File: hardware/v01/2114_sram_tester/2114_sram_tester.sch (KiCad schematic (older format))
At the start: 4 parts

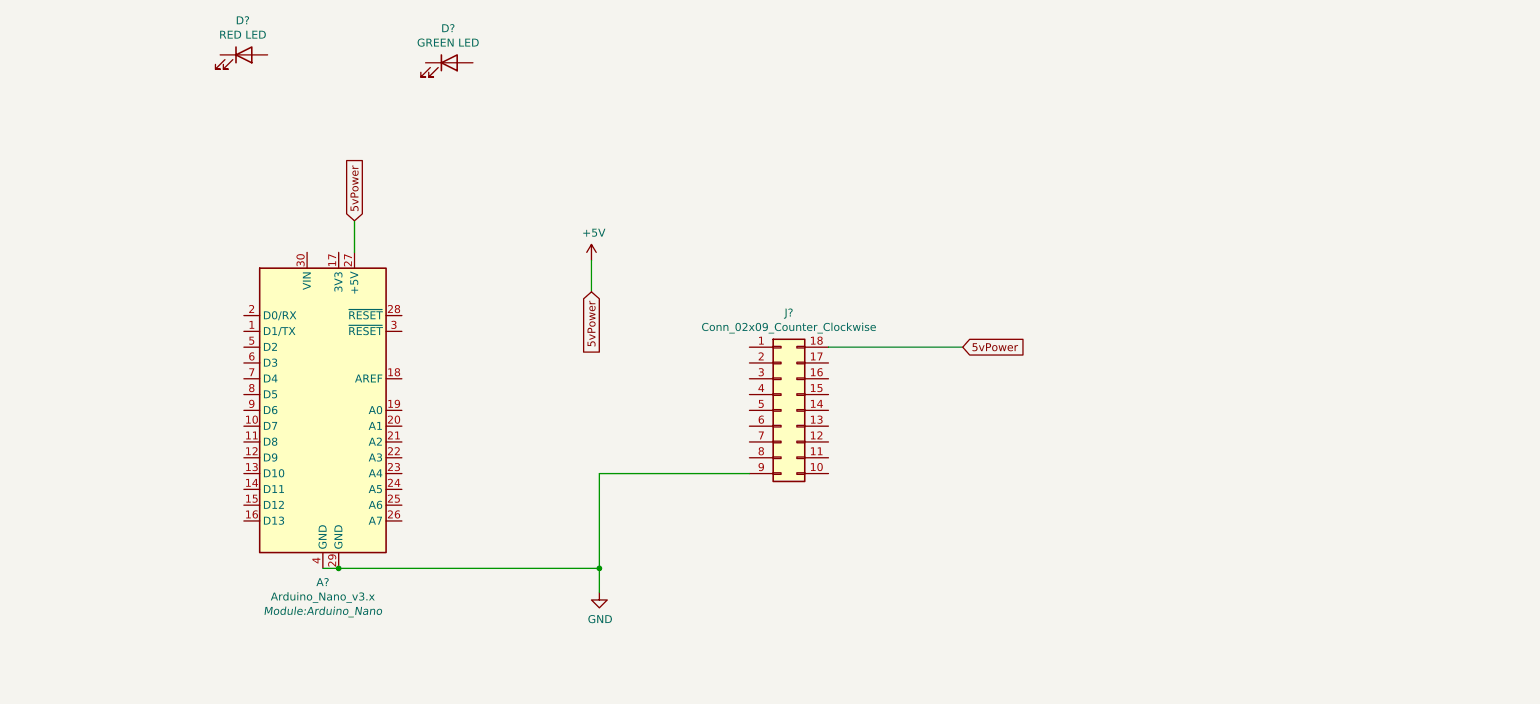
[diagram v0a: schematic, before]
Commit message: Added button code
Button added to stop/start tests
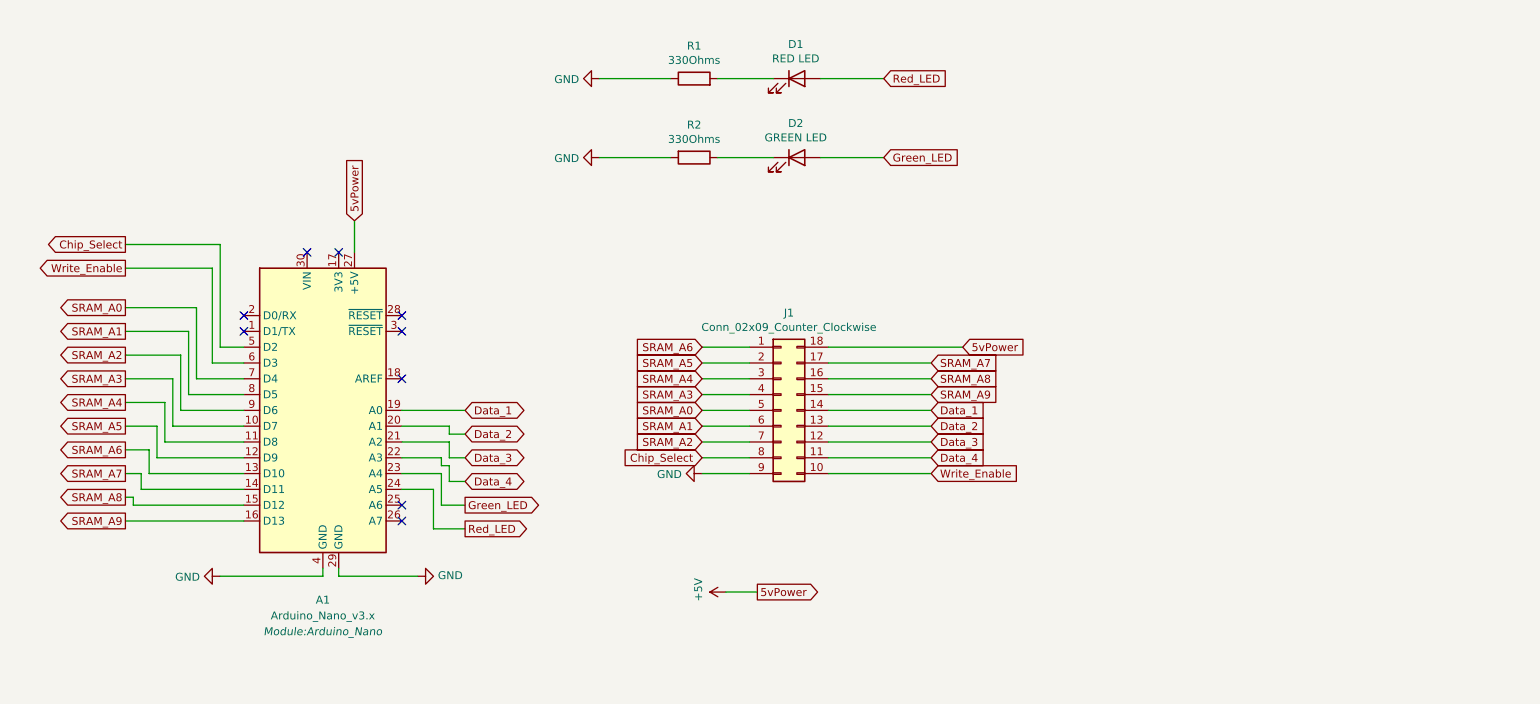
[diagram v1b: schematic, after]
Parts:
- added R1, R2: 330Ohms, Resistor_THT:R_Axial_DIN0309_L9.0mm_D3.2mm_P12.70mm_Horizontal, symbol Device:R
- gave numbers to parts that had none: 4
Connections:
- net GND: now also R1.1, R2.2
- net SRAM_A3: now reaches A1.10 (D7)
- net SRAM_A3: now also J1.4 (Pin_4)
- net SRAM_A4: now reaches A1.11 (D8)
- net SRAM_A4: now also J1.3 (Pin_3)
- net SRAM_A5: now reaches A1.12 (D9)
- net SRAM_A5: now also J1.2 (Pin_2)
- net SRAM_A6: now reaches A1.13 (D10)
- net SRAM_A6: now also J1.1 (Pin_1)
- net SRAM_A7: now reaches A1.14 (D11)
- net SRAM_A7: now also J1.17 (Pin_17)
- net SRAM_A8: now reaches A1.15 (D12)
- net SRAM_A8: now also J1.16 (Pin_16)
- net SRAM_A9: now reaches A1.16 (D13)
- net SRAM_A9: now also J1.15 (Pin_15)
- net Data_1: now reaches A1.19 (A0)
- net Data_1: now also J1.14 (Pin_14)
- net Data_2: now reaches A1.20 (A1)
- net Data_2: now also J1.13 (Pin_13)
- net Data_3: now reaches A1.21 (A2)
- net Data_3: now also J1.12 (Pin_12)
- net Data_4: now reaches A1.22 (A3)
- net Data_4: now also J1.11 (Pin_11)
- net Green_LED: now reaches A1.23 (A4)
- net Green_LED: now also D2.2 (A)
- net Red_LED: now reaches A1.24 (A5)
- net Red_LED: now also D1.2 (A)
- net Chip_Select: now reaches A1.5 (D2)
- net Chip_Select: now also J1.8 (Pin_8)
- net Write_Enable: now reaches A1.6 (D3)
- net Write_Enable: now also J1.10 (Pin_10)
- net SRAM_A0: now reaches A1.7 (D4)
- net SRAM_A0: now also J1.5 (Pin_5)
- net SRAM_A1: now reaches A1.8 (D5)
- net SRAM_A1: now also J1.6 (Pin_6)
- net SRAM_A2: now reaches A1.9 (D6)
- net SRAM_A2: now also J1.7 (Pin_7)
- net at D2.1 (K): now also R2.1
- net at D1.1 (K): now also R1.2
- no-connect marks 0 -> 9
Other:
- moved on the sheet: D1, D2

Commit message: Updated hardware
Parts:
- added R3: 10K Ohms, Resistor_THT:R_Axial_DIN0309_L9.0mm_D3.2mm_P12.70mm_Horizontal, symbol Device:R
- added SW1: SW_Push, Button_Switch_THT:SW_PUSH_6mm, symbol Switch:SW_Push
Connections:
- net +5V: now also R3.2
- net GND: now also SW1.1
- net Switch: now reaches A1.25 (A6)
- net Switch: now also R3.1, SW1.2
- no-connect marks 9 -> 8
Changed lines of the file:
@@
 L power:+5V #PWR0102
 U 1 1 60DFCCB0
-P 5000 4650
-F 0 "#PWR0102" H 5000 4500 50  0001 C CNN
-F 1 "+5V" H 5015 4823 50  0000 C CNN
-F 2 "" H 5000 4650 50  0001 C CNN
-F 3 "" H 5000 4650 50  0001 C CNN
-	1    5000 4650
+P 4800 5200
+F 0 "#PWR0102" H 4800 5050 50  0001 C CNN
+F 1 "+5V" H 4815 5373 50  0000 C CNN
+F 2 "" H 4800 5200 50  0001 C CNN
+F 3 "" H 4800 5200 50  0001 C CNN
+	1    4800 5200
 	0    -1   -1   0
 $EndComp
-Text GLabel 5200 4650 2    50   Output ~ 0
+Text GLabel 5000 5200 2    50   Output ~ 0
 5vPower
 Wire Wire Line
-	5000 4650 5200 4650
+	4800 5200 5000 5200
 Text GLabel 2650 2300 1    50   Input ~ 0
 5vPower
@@
 NoConn ~ 1950 3000
 NoConn ~ 1950 2900
-NoConn ~ 2950 4200
-NoConn ~ 2950 4100
 Wire Wire Line
 	2550 4500 2550 4550
@@
 Wire Wire Line
 	2450 4550 1800 4550
+Text GLabel 3350 4400 2    50   Input ~ 0
+Switch
+Wire Wire Line
+	3350 4400 3100 4400
+Wire Wire Line
+	3100 4400 3100 4100
+Wire Wire Line
+	3100 4100 2950 4100
+NoConn ~ 2950 4200
+Text GLabel 9650 3200 2    50   Input ~ 0
+Switch
+Text GLabel 9350 3850 3    50   Output ~ 0
+5vPower
+$Comp
+L Device:R R3
+U 1 1 60F72965
+P 9350 3500
+F 0 "R3" H 9420 3546 50  0000 L CNN
+F 1 "10K Ohms" H 9420 3455 50  0000 L CNN
+F 2 "Resistor_THT:R_Axial_DIN0309_L9.0mm_D3.2mm_P12.70mm_Horizontal" V 9280 3500 50  0001 C CNN
+F 3 "~" H 9350 3500 50  0001 C CNN
+	1    9350 3500
+	1    0    0    -1
+$EndComp
+Wire Wire Line
+	9350 3650 9350 3850
+Wire Wire Line
+	9350 3350 9350 3200
+Wire Wire Line
+	9350 3200 9650 3200
+$Comp
+L Switch:SW_Push SW1
+U 1 1 60F78C56
+P 8900 3200
+F 0 "SW1" H 8900 3485 50  0000 C CNN
+F 1 "SW_Push" H 8900 3394 50  0000 C CNN
+F 2 "Button_Switch_THT:SW_PUSH_6mm" H 8900 3400 50  0001 C CNN
+F 3 "~" H 8900 3400 50  0001 C CNN
+	1    8900 3200
+	1    0    0    -1
+$EndComp
+Wire Wire Line
+	9100 3200 9350 3200
+Connection ~ 9350 3200
+$Comp
+L power:GND #PWR01
+U 1 1 60F7B889
+P 8400 3200
+F 0 "#PWR01" H 8400 2950 50  0001 C CNN
+F 1 "GND" V 8405 3072 50  0000 R CNN
+F 2 "" H 8400 3200 50  0001 C CNN
+F 3 "" H 8400 3200 50  0001 C CNN
+	1    8400 3200
+	0    1    1    0
+$EndComp
+Wire Wire Line
+	8700 3200 8400 3200
 $EndSCHEMATC
